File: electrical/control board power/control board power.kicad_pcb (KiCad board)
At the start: 2 copper layers, 72.4 x 149.8 mm, 0 parts

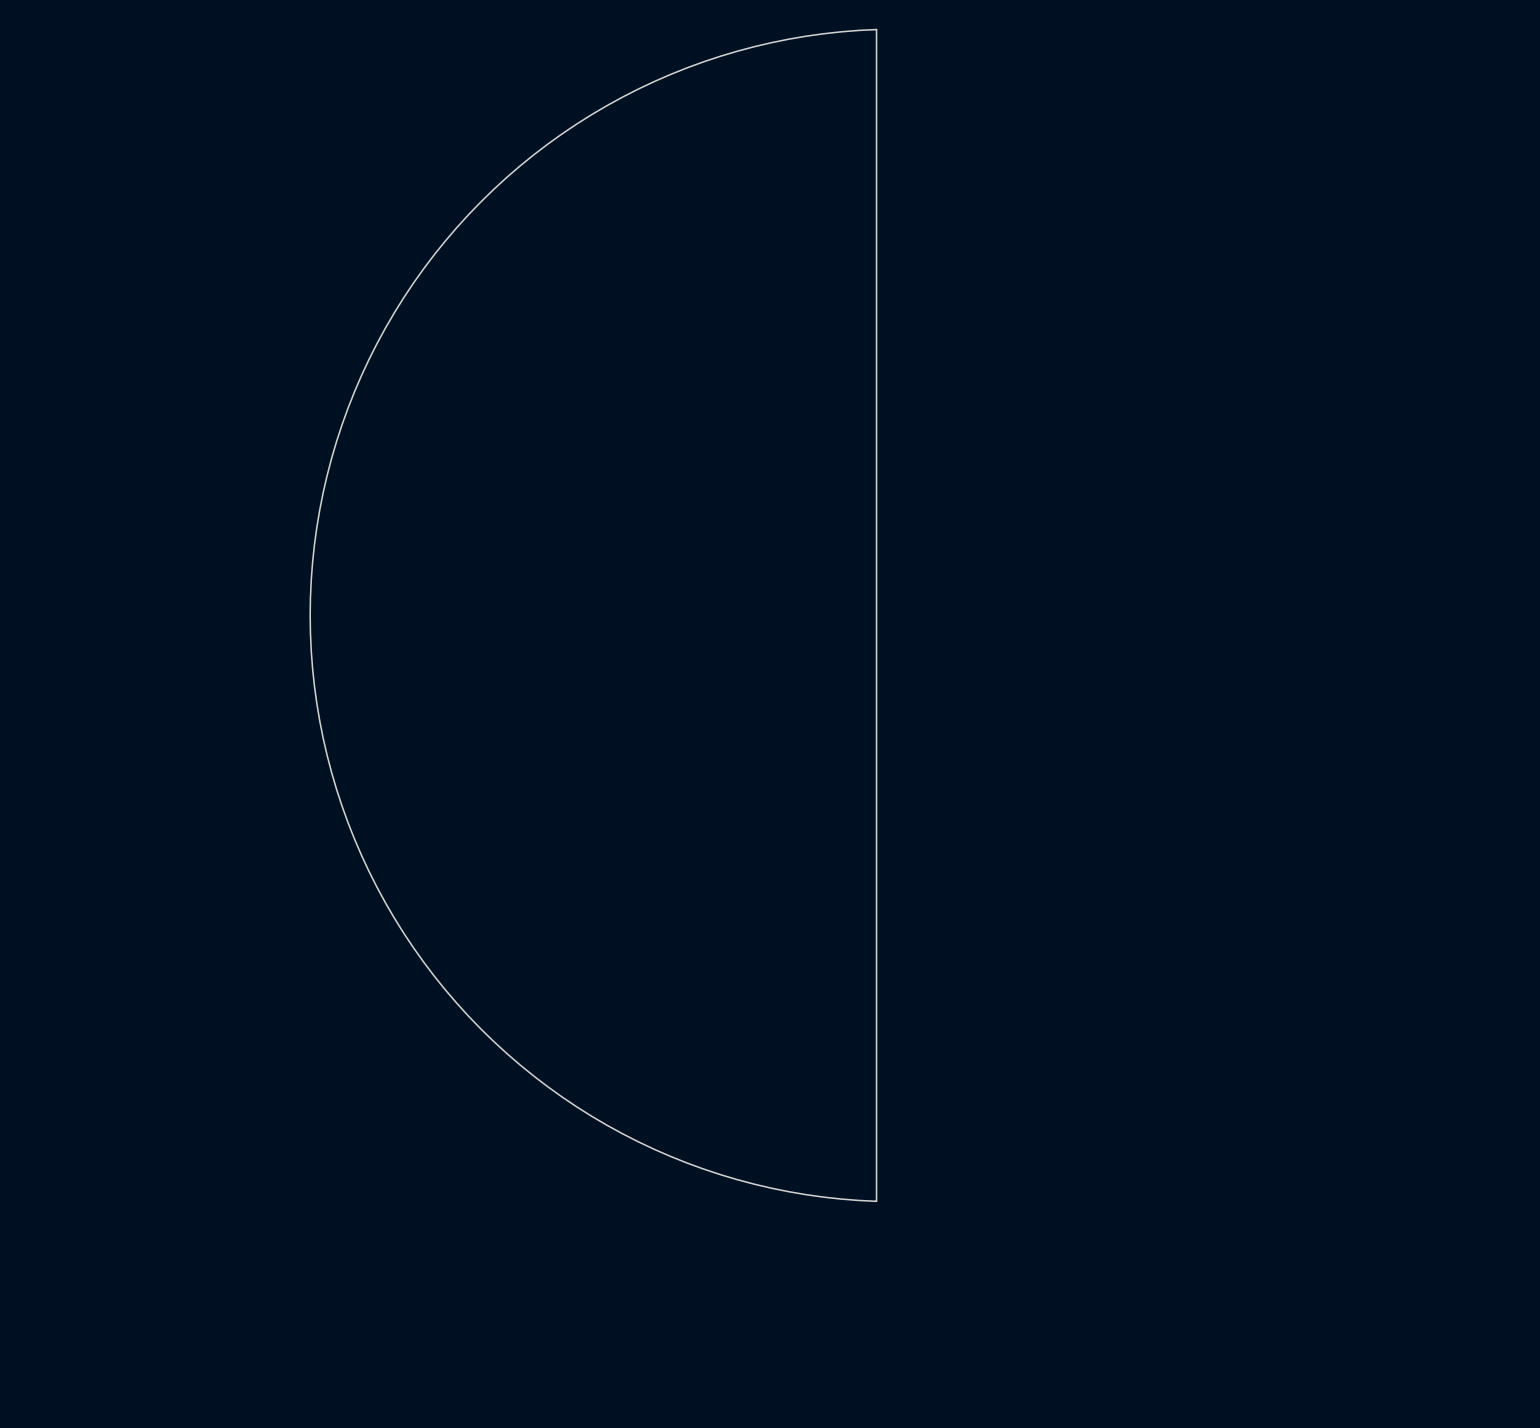
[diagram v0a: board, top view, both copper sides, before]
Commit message: made a footprint with long pads and a hole in the middle
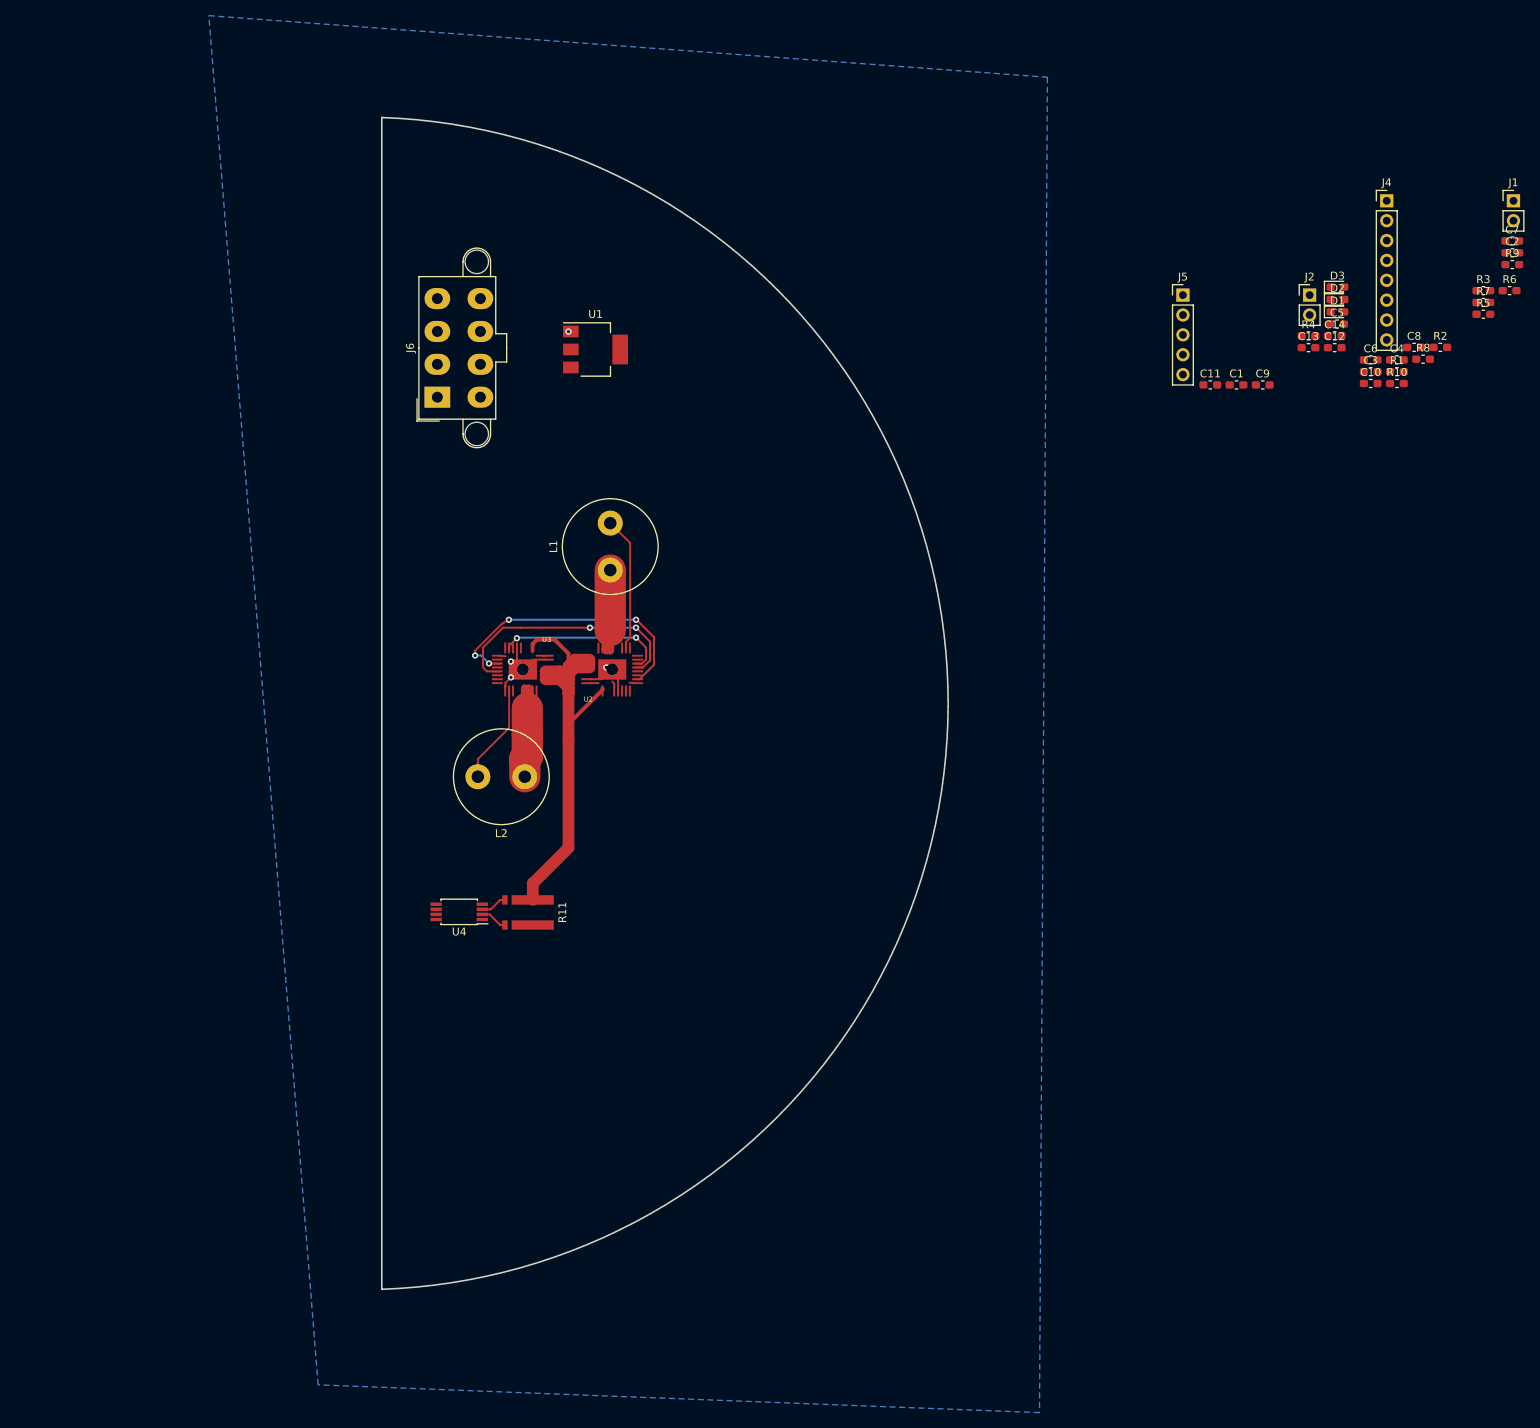
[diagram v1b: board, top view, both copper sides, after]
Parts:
- added C1: 10uF, Capacitor_SMD:C_0603_1608Metric_Pad1.05x0.95mm_HandSolder, F.Cu at (198.2, 74.4)
- added C10: 2.2nF, Capacitor_SMD:C_0603_1608Metric_Pad1.05x0.95mm_HandSolder, F.Cu at (215.3, 74.2)
- added C11: 100pF, Capacitor_SMD:C_0603_1608Metric_Pad1.05x0.95mm_HandSolder, F.Cu at (194.8, 74.4)
- added C12: 22uF, Capacitor_SMD:C_0603_1608Metric_Pad1.05x0.95mm_HandSolder, F.Cu at (210.7, 69.6)
- added C13: 22uF, Capacitor_SMD:C_0603_1608Metric_Pad1.05x0.95mm_HandSolder, F.Cu at (207.4, 69.6)
- added C14: C_Small, Capacitor_SMD:C_0603_1608Metric_Pad1.05x0.95mm_HandSolder, F.Cu at (210.7, 68.1)
- added C2: 10uF, Capacitor_SMD:C_0603_1608Metric_Pad1.05x0.95mm_HandSolder, F.Cu at (233.4, 57.5)
- added C3: 4.7uF, Capacitor_SMD:C_0603_1608Metric_Pad1.05x0.95mm_HandSolder, F.Cu at (215.3, 72.7)
- added C4: 4.7uF, Capacitor_SMD:C_0603_1608Metric_Pad1.05x0.95mm_HandSolder, F.Cu at (218.7, 71.2)
- added C5: 1uF, Capacitor_SMD:C_0603_1608Metric_Pad1.05x0.95mm_HandSolder, F.Cu at (211.0, 66.6)
- added C6: .1uF, Capacitor_SMD:C_0603_1608Metric_Pad1.05x0.95mm_HandSolder, F.Cu at (215.3, 71.2)
- added C7: 1uF, Capacitor_SMD:C_0603_1608Metric_Pad1.05x0.95mm_HandSolder, F.Cu at (233.4, 56.0)
- added C8: .1uF, Capacitor_SMD:C_0603_1608Metric_Pad1.05x0.95mm_HandSolder, F.Cu at (220.9, 69.6)
- added C9: 10pF, Capacitor_SMD:C_0603_1608Metric_Pad1.05x0.95mm_HandSolder, F.Cu at (201.5, 74.4)
- added D1: LED, LED_SMD:LED_0603_1608Metric_Pad1.05x0.95mm_HandSolder, F.Cu at (211.1, 65.0)
- added D2: LED, LED_SMD:LED_0603_1608Metric_Pad1.05x0.95mm_HandSolder, F.Cu at (211.1, 63.5)
- added D3: LED, LED_SMD:LED_0603_1608Metric_Pad1.05x0.95mm_HandSolder, F.Cu at (211.1, 61.9)
- added J1: 48V_IN, Connector_PinHeader_2.54mm:PinHeader_1x02_P2.54mm_Vertical, F.Cu at (233.6, 50.8)
- added J2: 5V, Connector_PinHeader_2.54mm:PinHeader_1x02_P2.54mm_Vertical, F.Cu at (207.5, 62.9)
- added J4: Conn_01x08, Connector_PinHeader_2.54mm:PinHeader_1x08_P2.54mm_Vertical, F.Cu at (217.4, 50.8)
- added J5: Conn_01x05, Connector_PinHeader_2.54mm:PinHeader_1x05_P2.54mm_Vertical, F.Cu at (191.3, 62.9)
- added J6: Power_Connector, Connector_Molex:Molex_Mini-Fit_Jr_5566-08A2_2x04_P4.20mm_Vertical, F.Cu at (96.0, 75.9)
- added L1: 33uH, Inductor_THT:L_Radial_D12.0mm_P6.00mm_MuRATA_1900R, F.Cu at (118.1, 98.0)
- added L2: 33uH, Inductor_THT:L_Radial_D12.0mm_P6.00mm_MuRATA_1900R, F.Cu at (107.2, 124.5)
- added R1: R_Small, Resistor_SMD:R_0603_1608Metric_Pad1.05x0.95mm_HandSolder, F.Cu at (218.7, 72.7)
- added R10: 5.11k, Resistor_SMD:R_0603_1608Metric_Pad1.05x0.95mm_HandSolder, F.Cu at (218.7, 74.2)
- added R11: 1m, footprints:FC4L64, F.Cu at (108.2, 141.8)
- added R2: R_Small, Resistor_SMD:R_0603_1608Metric_Pad1.05x0.95mm_HandSolder, F.Cu at (224.2, 69.6)
- added R3: R_Small, Resistor_SMD:R_0603_1608Metric_Pad1.05x0.95mm_HandSolder, F.Cu at (229.7, 62.3)
- added R4: 10k, Resistor_SMD:R_0603_1608Metric_Pad1.05x0.95mm_HandSolder, F.Cu at (207.4, 68.1)
- added R5: 10k, Resistor_SMD:R_0603_1608Metric_Pad1.05x0.95mm_HandSolder, F.Cu at (229.7, 65.3)
- added R6: 10k, Resistor_SMD:R_0603_1608Metric_Pad1.05x0.95mm_HandSolder, F.Cu at (233.1, 62.3)
- added R7: 100k, Resistor_SMD:R_0603_1608Metric_Pad1.05x0.95mm_HandSolder, F.Cu at (229.7, 63.8)
- added R8: 4.02k, Resistor_SMD:R_0603_1608Metric_Pad1.05x0.95mm_HandSolder, F.Cu at (222.0, 71.1)
- added R9: 10k, Resistor_SMD:R_0603_1608Metric_Pad1.05x0.95mm_HandSolder, F.Cu at (233.4, 59.0)
- added U1: LD1117S33TR_SOT223, Package_TO_SOT_SMD:SOT-223-3_TabPin2, F.Cu at (116.2, 69.8)
- added U2: LTC7103-LT7103, footprints:LTC7103_long_pads_hole, F.Cu at (118.4, 110.7)
- added U3: LTC7103-LT7103, footprints:LTC7103_long_pads_hole, F.Cu at (106.9, 110.7)
- added U4: INA240-INA240, Package_SO:TSSOP-8_4.4x3mm_P0.65mm, F.Cu at (98.8, 141.7)
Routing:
- net +12V: track 0.00 -> 70.6 mm
- net Net-(U2-Pad12): track 0.00 -> 36.3 mm, vias 0 -> 4
- net Net-(U2-Pad15): track 0.00 -> 32.8 mm, vias 0 -> 2
- net +5V: track 0.00 -> 30.5 mm
- net Net-(C10-Pad2): track 0.00 -> 22.2 mm, vias 0 -> 2
- net Net-(C8-Pad2): track 0.00 -> 17.0 mm
- net Net-(C6-Pad2): track 0.00 -> 16.0 mm
- net GND: track 0.00 -> 13.0 mm, vias 0 -> 4
- net Net-(R11-Pad2): track 0.00 -> 3.46 mm
- net Net-(R11-Pad3): track 0.00 -> 3.39 mm
- added copper zone on B.Cu, net GND
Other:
- outline, holes or cut-outs redrawn

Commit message: made a mess
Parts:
- moved U1 9.10 mm to (112.4, 78.1), turned to 180 degrees
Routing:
- net +12V: track 70.6 -> 201.8 mm
- net +5V: track 30.5 -> 149.2 mm, vias 0 -> 2
- net +3V3: track 0.00 -> 15.7 mm, vias 0 -> 8
- net GND: track 13.0 -> 22.6 mm, vias 4 -> 21
- net Net-(C6-Pad2): track 16.0 -> 18.7 mm
- net Net-(C8-Pad2): track 17.0 -> 18.4 mm
- net (no net): vias 0 -> 6

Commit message: fixed the mess
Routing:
- net GND: track 22.6 -> 21.8 mm, vias 21 -> 26
- net (no net): vias 6 -> 2

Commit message: fixed the mess
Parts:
- C8: moved to B.Cu
- moved R7 137.7 mm to (101.3, 113.8), turned to 270 degrees
- moved C13 123.5 mm to (95.8, 122.5), turned to 270 degrees
- moved C8 121.2 mm to (109.0, 116.1), turned to 270 degrees
- moved C4 116.7 mm to (110.7, 115.7), turned to 270 degrees
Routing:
- net Net-(R7-Pad1): track 0.00 -> 11.4 mm, vias 0 -> 2
- net Net-(C7-Pad1): track 0.00 -> 7.39 mm
- net +5V: track 149.2 -> 152.4 mm, vias 2 -> 4
- net Net-(C8-Pad1): track 0.00 -> 2.60 mm, vias 0 -> 1
- net +12V: track 201.8 -> 204.2 mm
- net Net-(U2-Pad12): track 36.3 -> 37.0 mm, vias 4 -> 2
- net Net-(U2-Pad15): track 32.8 -> 33.5 mm, vias 2 -> 4
- net Net-(C8-Pad2): vias 0 -> 1
- net GND: vias 26 -> 28
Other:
- board text added: "input capacitor footprints may need to be changed if capacitors don't have the proper voltage rating"

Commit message: stuff
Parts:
- C3: moved to B.Cu
- moved C7 146.6 mm to (100.1, 116.8), turned to 180 degrees
- moved R8 114.1 mm to (117.3, 116.6), turned to 270 degrees
- moved C3 107.9 mm to (114.6, 111.3), turned to 270 degrees
- moved C6 107.6 mm to (112.3, 102.1)
- moved C5 101.2 mm to (122.9, 116.4), turned to 270 degrees
- moved R10 100.3 mm to (126.9, 114.6)
- moved C10 96.1 mm to (126.7, 111.5)
- moved C9 91.6 mm to (120.1, 116.4), turned to 270 degrees
- moved C11 80.5 mm to (126.9, 117.6)
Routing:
- net Net-(C10-Pad2): track 22.2 -> 42.2 mm, vias 2 -> 3
- net Net-(C5-Pad1): track 0.00 -> 17.8 mm, vias 0 -> 2
- net Net-(C6-Pad1): track 0.00 -> 8.40 mm
- net Net-(C6-Pad2): track 18.7 -> 24.5 mm
- net Net-(R8-Pad1): track 0.00 -> 4.07 mm
- net Net-(C10-Pad1): track 0.00 -> 3.09 mm
- net Net-(C9-Pad1): track 0.00 -> 2.44 mm
- net Net-(C7-Pad1): track 7.39 -> 9.78 mm
- net +12V: vias 0 -> 1
- net GND: vias 28 -> 36
- net (no net): vias 2 -> 0

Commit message: more stuff
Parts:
- moved C14 138.7 mm to (92.7, 141.0), turned to 270 degrees
- moved C2 127.0 mm to (109.2, 84.1), turned to 270 degrees
- moved R2 126.1 mm to (99.1, 85.3)
- moved R1 120.7 mm to (99.1, 88.9)
- moved R3 120.6 mm to (109.5, 53.6)
- moved D1 118.7 mm to (94.7, 88.9)
- moved D2 118.4 mm to (94.7, 85.3)
- moved D3 97.4 mm to (114.0, 53.6), turned to 180 degrees
- moved C1 79.2 mm to (119.1, 79.0), turned to 270 degrees
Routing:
- net +3V3: track 15.7 -> 105.6 mm
- net +5V: track 152.4 -> 161.9 mm
- net +12V: track 204.2 -> 212.2 mm
- net Net-(D3-Pad2): track 0.00 -> 2.82 mm
- net Net-(D2-Pad2): track 0.00 -> 2.57 mm
- net Net-(D1-Pad2): track 0.00 -> 2.57 mm
- net GND: track 21.8 -> 22.9 mm, vias 36 -> 42
